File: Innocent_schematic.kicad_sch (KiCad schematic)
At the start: 59 parts, among them IC1 MP2338GTL-Z, J1 Conn_02x16_Top_Bottom, P1 USB_C_Plug_USB2.0, Q1 TIP42C, Q2 MMBT5551, Q3 MMBT5551, Q4 TIP42C, SW1 SPDT, U1 CH224K, U2 TP4056-42-ESOP8, U3 MP3423GG-Z, U4 RT6150AGQW, U5 INA219AxD, U6 DRV8833PWP, U7 DRV8833PWP

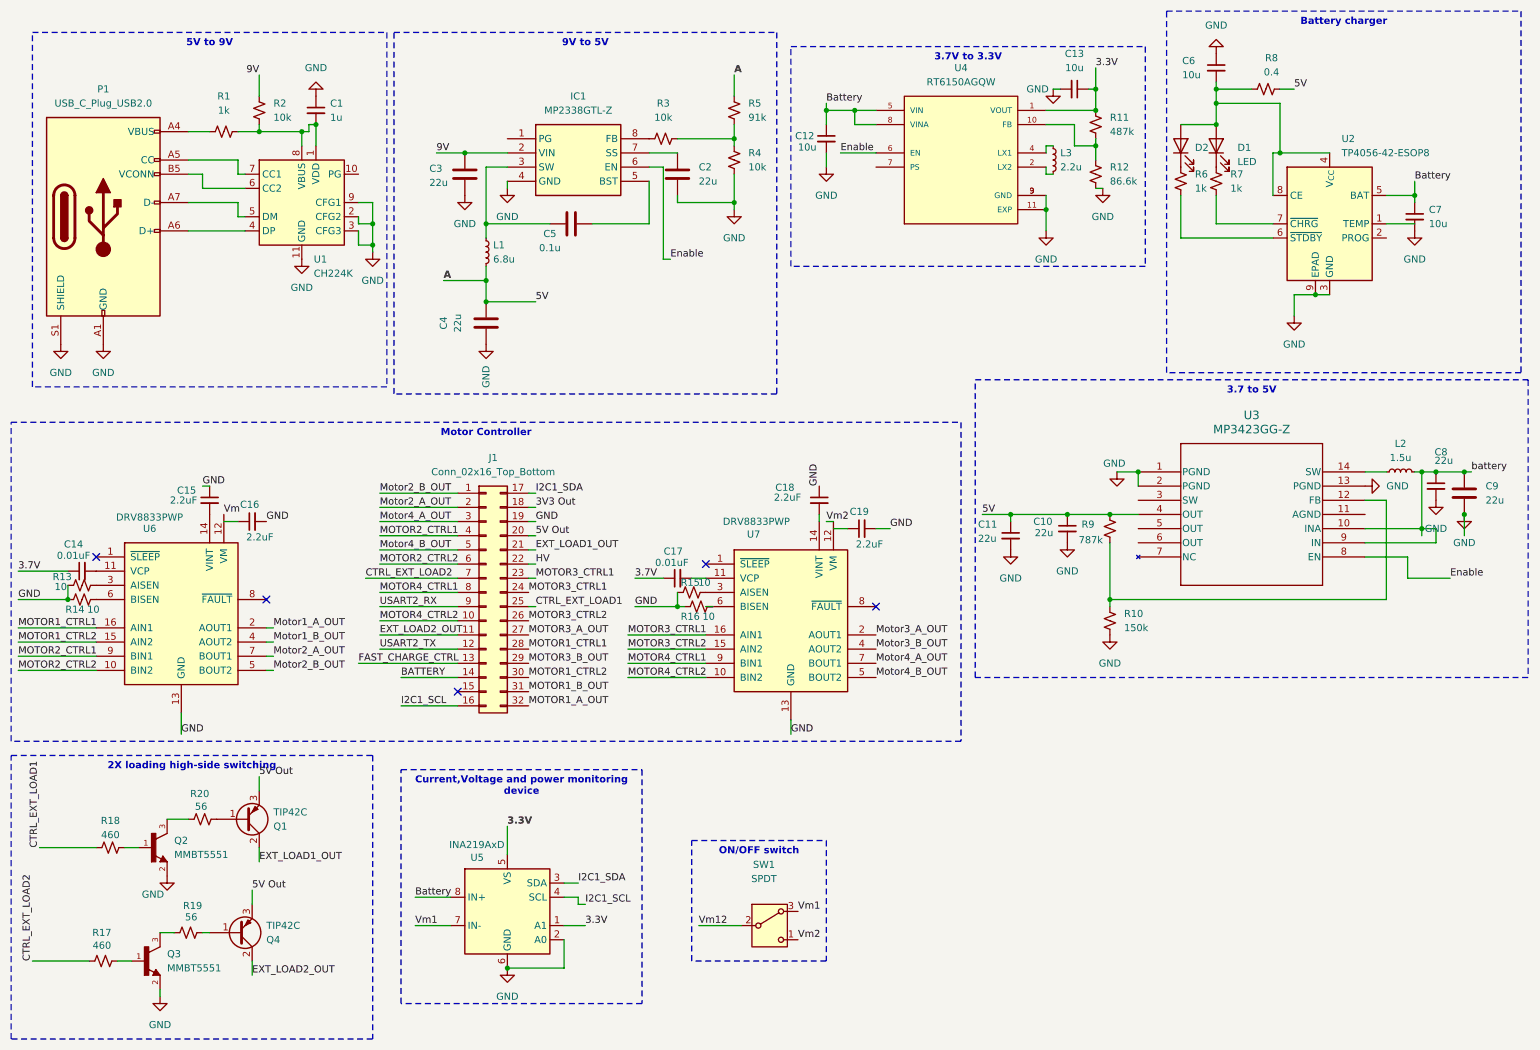
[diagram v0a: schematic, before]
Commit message: this version has pin numbers modified as we have analized and agreed
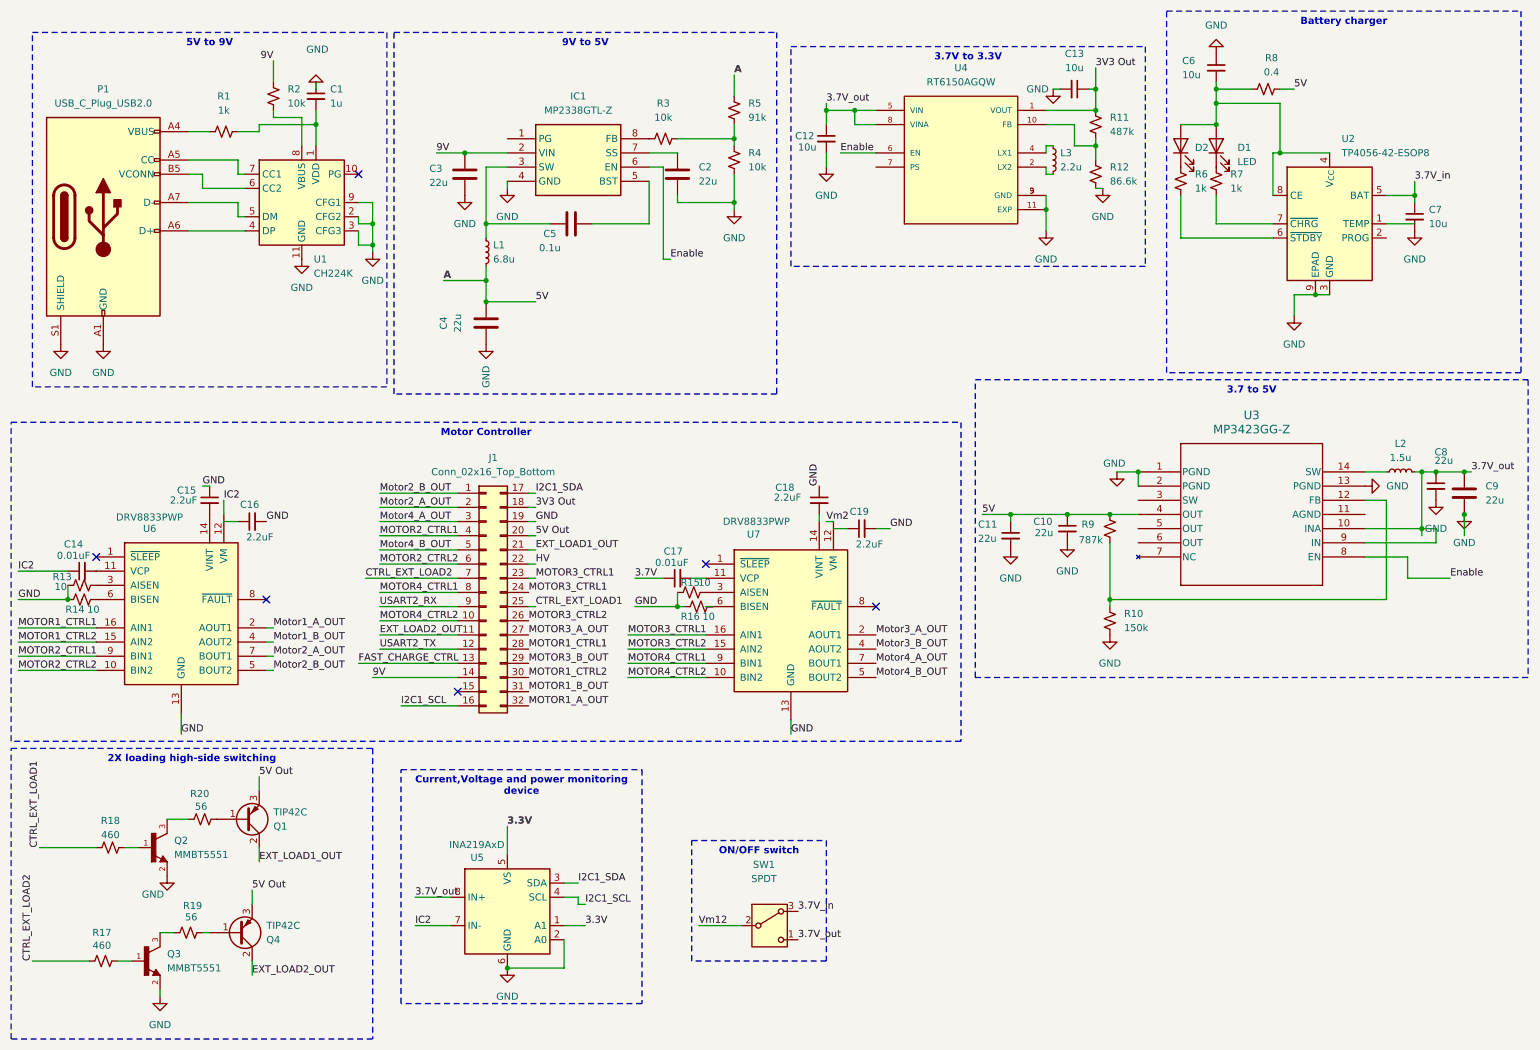
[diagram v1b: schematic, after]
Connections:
- net BATTERY is gone; now on net 9V: J1.14 (Pin_14)
- net battery is gone; now on net 3.7V_out: C8.1, C9.1, L2.2, U3.10 (INA), U3.9 (IN)
- net 3.3V: no longer C13.1, R11.1, U4.1 (VOUT)
- net 3.7V: no longer C14.1
- net 3V3 Out: now also C13.1, R11.1, U4.1 (VOUT)
- net Vm2: no longer SW1.1 (C)
- net at C1.2, R1.2, U1.1 (VDD): no longer R2.2, U1.8 (VBUS)
- net Battery renamed 3.7V_out
- net 3.7V_out: now also SW1.1 (C); no longer C7.1, U2.5 (BAT)
- net Vm renamed IC2
- net IC2: now also C14.1, U5.7 (IN-)
- net Vm1 renamed 3.7V_in
- net 3.7V_in: now also C7.1, U2.5 (BAT); no longer U5.7 (IN-)
- new net: R2.2, U1.8 (VBUS)
- no-connect marks 5 -> 6
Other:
- company: (none) -> University of Cape Town
- title: (none) -> EEE3088F_Micromouse_power_module
- moved on the sheet: C1, R2
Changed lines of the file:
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@@
 	(generator_version "9.0")
 	(paper "A4")
+	(title_block
+		(title "EEE3088F_Micromouse_power_module")
+		(date "2025-03-24")
+		(rev "R5")
+		(company "University of Cape Town")
+		(comment 1 "Authors: Rasekoai Mokose and Innocent Mkhonta")
+	)
 	(text_box "Battery charger"
 		(exclude_from_sim no)
@@
 	(text_box "2X loading high-side switching "
 		(exclude_from_sim no)
-		(at 12.7 146.05 0)
-		(size 64.77 50.8)
+		(at 12.7 144.78 0)
+		(size 64.77 52.07)
 		(margins 0.9525 0.9525 0.9525 0.9525)
 		(stroke
@@
 	)
 	(junction
-		(at 64.77 34.29)
-		(diameter 0)
-		(color 0 0 0 0)
-	)
-	(junction
 		(at 207.01 30.48)
 		(diameter 0)
@@
 	)
 	(junction
-		(at 57.15 34.29)
-		(diameter 0)
-		(color 0 0 0 0)
-	)
-	(junction
 		(at 246.38 63.5)
 		(diameter 0)
@@
 	)
 	(no_connect
+		(at 74.93 41.91)
+	)
+	(no_connect
 		(at 92.71 134.62)
 	)
@@
 	(wire
 		(pts
+			(xy 64.77 31.75) (xy 64.77 36.83)
+		)
+		(stroke
+			(width 0)
+			(type default)
+		)
+	)
+	(wire
+		(pts
 			(xy 123.19 127) (xy 137.16 127)
 		)
@@
 	(wire
 		(pts
-			(xy 64.77 36.83) (xy 64.77 34.29)
+			(xy 59.69 31.75) (xy 59.69 30.48)
 		)
 		(stroke
@@
 	(wire
 		(pts
-			(xy 64.77 34.29) (xy 57.15 34.29)
-		)
-		(stroke
-			(width 0)
-			(type default)
-		)
-	)
-	(wire
-		(pts
 			(xy 59.69 123.19) (xy 58.42 123.19)
 		)
@@
 	(wire
 		(pts
+			(xy 59.69 21.59) (xy 59.69 25.4)
+		)
+		(stroke
+			(width 0)
+			(type default)
+		)
+	)
+	(wire
+		(pts
 			(xy 116.84 50.8) (xy 127 50.8)
 		)
@@
 	(wire
 		(pts
+			(xy 67.31 30.48) (xy 67.31 33.02)
+		)
+		(stroke
+			(width 0)
+			(type default)
+		)
+	)
+	(wire
+		(pts
 			(xy 142.24 33.02) (xy 142.24 35.56)
 		)
@@
 	(wire
 		(pts
-			(xy 66.04 34.29) (xy 64.77 34.29)
-		)
-		(stroke
-			(width 0)
-			(type default)
-		)
-	)
-	(wire
-		(pts
 			(xy 134.62 114.3) (xy 137.16 114.3)
 		)
@@
 	(wire
 		(pts
+			(xy 67.31 25.4) (xy 67.31 26.67)
+		)
+		(stroke
+			(width 0)
+			(type default)
+		)
+	)
+	(wire
+		(pts
 			(xy 106.68 101.6) (xy 105.41 101.6)
 		)
@@
 	(wire
 		(pts
-			(xy 199.39 26.67) (xy 200.66 26.67)
+			(xy 59.69 31.75) (xy 64.77 31.75)
 		)
 		(stroke
@@
 	(wire
 		(pts
-			(xy 158.75 33.02) (xy 158.75 30.48)
+			(xy 199.39 26.67) (xy 200.66 26.67)
 		)
 		(stroke
@@
 	(wire
 		(pts
-			(xy 264.16 43.18) (xy 264.16 45.72)
+			(xy 158.75 33.02) (xy 158.75 30.48)
 		)
 		(stroke
@@
 	(wire
 		(pts
-			(xy 57.15 24.13) (xy 57.15 27.94)
+			(xy 264.16 43.18) (xy 264.16 45.72)
 		)
 		(stroke
@@
 	(wire
 		(pts
+			(xy 50.8 100.33) (xy 50.8 102.87)
+		)
+		(stroke
+			(width 0)
+			(type default)
+		)
+	)
+	(wire
+		(pts
 			(xy 273.05 95.25) (xy 274.32 95.25)
 		)
@@
 	(wire
 		(pts
+			(xy 57.15 33.02) (xy 67.31 33.02)
+		)
+		(stroke
+			(width 0)
+			(type default)
+		)
+	)
+	(wire
+		(pts
 			(xy 259.08 118.11) (xy 209.55 118.11)
 		)
@@
 	(wire
 		(pts
-			(xy 66.04 33.02) (xy 67.31 33.02)
-		)
-		(stroke
-			(width 0)
-			(type default)
-		)
-	)
-	(wire
-		(pts
 			(xy 142.24 35.56) (xy 142.24 36.83)
 		)
@@
 	(wire
 		(pts
-			(xy 66.04 33.02) (xy 66.04 34.29)
-		)
-		(stroke
-			(width 0)
-			(type default)
-		)
-	)
-	(wire
-		(pts
 			(xy 13.97 118.11) (xy 22.86 118.11)
 		)
@@
 	(wire
 		(pts
-			(xy 82.55 132.08) (xy 92.71 132.08)
+			(xy 77.47 132.08) (xy 92.71 132.08)
 		)
 		(stroke
@@
 		)
 	)
+	(label "9V"
+		(at 59.69 21.59 180)
+		(effects
+			(font
+				(size 1.27 1.27)
+			)
+			(justify right bottom)
+		)
+	)
 	(label "Motor4_B_OUT"
 		(at 167.64 132.08 0)
@@
 		)
 	)
-	(label "Battery"
+	(label "3.7V_in"
 		(at 264.16 43.18 0)
 		(effects
@@
 		)
 	)
-	(label "Vm1"
+	(label "3.7V_in"
 		(at 153.67 173.99 0)
 		(effects
@@
 		)
 	)
-	(label "Vm"
-		(at 50.8 102.87 0)
+	(label "IC2"
+		(at 50.8 100.33 0)
 		(effects
 			(font
@@
 		)
 	)
-	(label "Battery"
+	(label "3.7V_out"
 		(at 85.09 171.45 0)
 		(effects
@@
 		)
 	)
-	(label "Battery"
+	(label "3.7V_out"
 		(at 158.75 29.21 0)
 		(effects
@@
 		)
 	)
-	(label "3.3V"
+	(label "3V3 Out"
 		(at 207.01 22.86 0)
 		(effects
@@
 		)
 	)
-	(label "Vm2"
+	(label "3.7V_out"
 		(at 153.67 179.07 0)
 		(effects
@@
 		)
 	)
-	(label "3.7V"
+	(label "IC2"
 		(at 13.97 113.03 0)
 		(effects
@@
 		)
 	)
-	(label "Vm1"
+	(label "IC2"
 		(at 85.09 176.53 0)
 		(effects
@@
 		)
 	)
-	(label "9V"
-		(at 57.15 24.13 180)
-		(effects
-			(font
-				(size 1.27 1.27)
-			)
-			(justify right bottom)
-		)
-	)
-	(label "battery"
+	(label "3.7V_out"
 		(at 274.32 95.25 0)
 		(effects
@@
 		)
 	)
-	(label "BATTERY"
-		(at 82.55 132.08 0)
+	(label "9V"
+		(at 77.47 132.08 0)
 		(effects
 			(font
@@
 	(symbol
 		(lib_id "Device:C_Small")
-		(at 67.31 30.48 0)
+		(at 67.31 27.94 0)
 		(unit 1)
 		(exclude_from_sim no)
@@
 		(fields_autoplaced yes)
 		(property "Reference" "C1"
-			(at 69.85 29.2162 0)
+			(at 69.85 26.6762 0)
 			(effects
 				(font
@@
 		)
 		(property "Value" "1u"
-			(at 69.85 31.7562 0)
+			(at 69.85 29.2162 0)
 			(effects
 				(font
@@
 		)
 		(property "Footprint" ""
-			(at 67.31 30.48 0)
+			(at 67.31 27.94 0)
 			(effects
 				(font
@@
 		)
 		(property "Datasheet" "~"
-			(at 67.31 30.48 0)
+			(at 67.31 27.94 0)
 			(effects
 				(font
@@
 		)
 		(property "Description" "Unpolarized capacitor, small symbol"
-			(at 67.31 30.48 0)
+			(at 67.31 27.94 0)
 			(effects
 				(font
@@
 	(symbol
 		(lib_id "power:GND")
-		(at 67.31 27.94 180)
+		(at 67.31 26.67 180)
 		(unit 1)
 		(exclude_from_sim no)
@@
 		(on_board yes)
 		(dnp no)
-		(fields_autoplaced yes)
 		(property "Reference" "#PWR02"
-			(at 67.31 21.59 0)
+			(at 67.31 20.32 0)
 			(effects
 				(font
@@
 		)
 		(property "Value" "GND"
-			(at 67.31 22.86 0)
+			(at 67.564 19.558 0)
 			(effects
 				(font
@@
 		)
 		(property "Footprint" ""
-			(at 67.31 27.94 0)
+			(at 67.31 26.67 0)
 			(effects
 				(font
@@
 		)
 		(property "Datasheet" ""
-			(at 67.31 27.94 0)
+			(at 67.31 26.67 0)
 			(effects
 				(font
@@
 		)
 		(property "Description" "Power symbol creates a global label with name \"GND\" , ground"
-			(at 67.31 27.94 0)
+			(at 67.31 26.67 0)
 			(effects
 				(font
@@
 	(symbol
 		(lib_id "Device:R_Small_US")
-		(at 57.15 30.48 0)
+		(at 59.69 27.94 0)
 		(unit 1)
 		(exclude_from_sim no)
@@
 		(fields_autoplaced yes)
 		(property "Reference" "R2"
-			(at 59.69 29.2099 0)
+			(at 62.23 26.6699 0)
 			(effects
 				(font
@@
 		)
 		(property "Value" "10k"
-			(at 59.69 31.7499 0)
+			(at 62.23 29.2099 0)
 			(effects
 				(font
@@
 		)
 		(property "Footprint" ""
-			(at 57.15 30.48 0)
+			(at 59.69 27.94 0)
 			(effects
 				(font
@@
 		)
 		(property "Datasheet" "~"
-			(at 57.15 30.48 0)
+			(at 59.69 27.94 0)
 			(effects
 				(font
@@
 		)
 		(property "Description" "Resistor, small US symbol"
-			(at 57.15 30.48 0)
+			(at 59.69 27.94 0)
 			(effects
 				(font
@@
 		)
 		(instances
-			(project ""
+			(project "Innocent_schematic"
 				(path "/0ebc6b21-534b-4d26-a743-fadd30dffdd1"
 					(reference "R2")

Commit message: i have added the footprints to the folder and assigned most components, i am just left with JST pin and USB
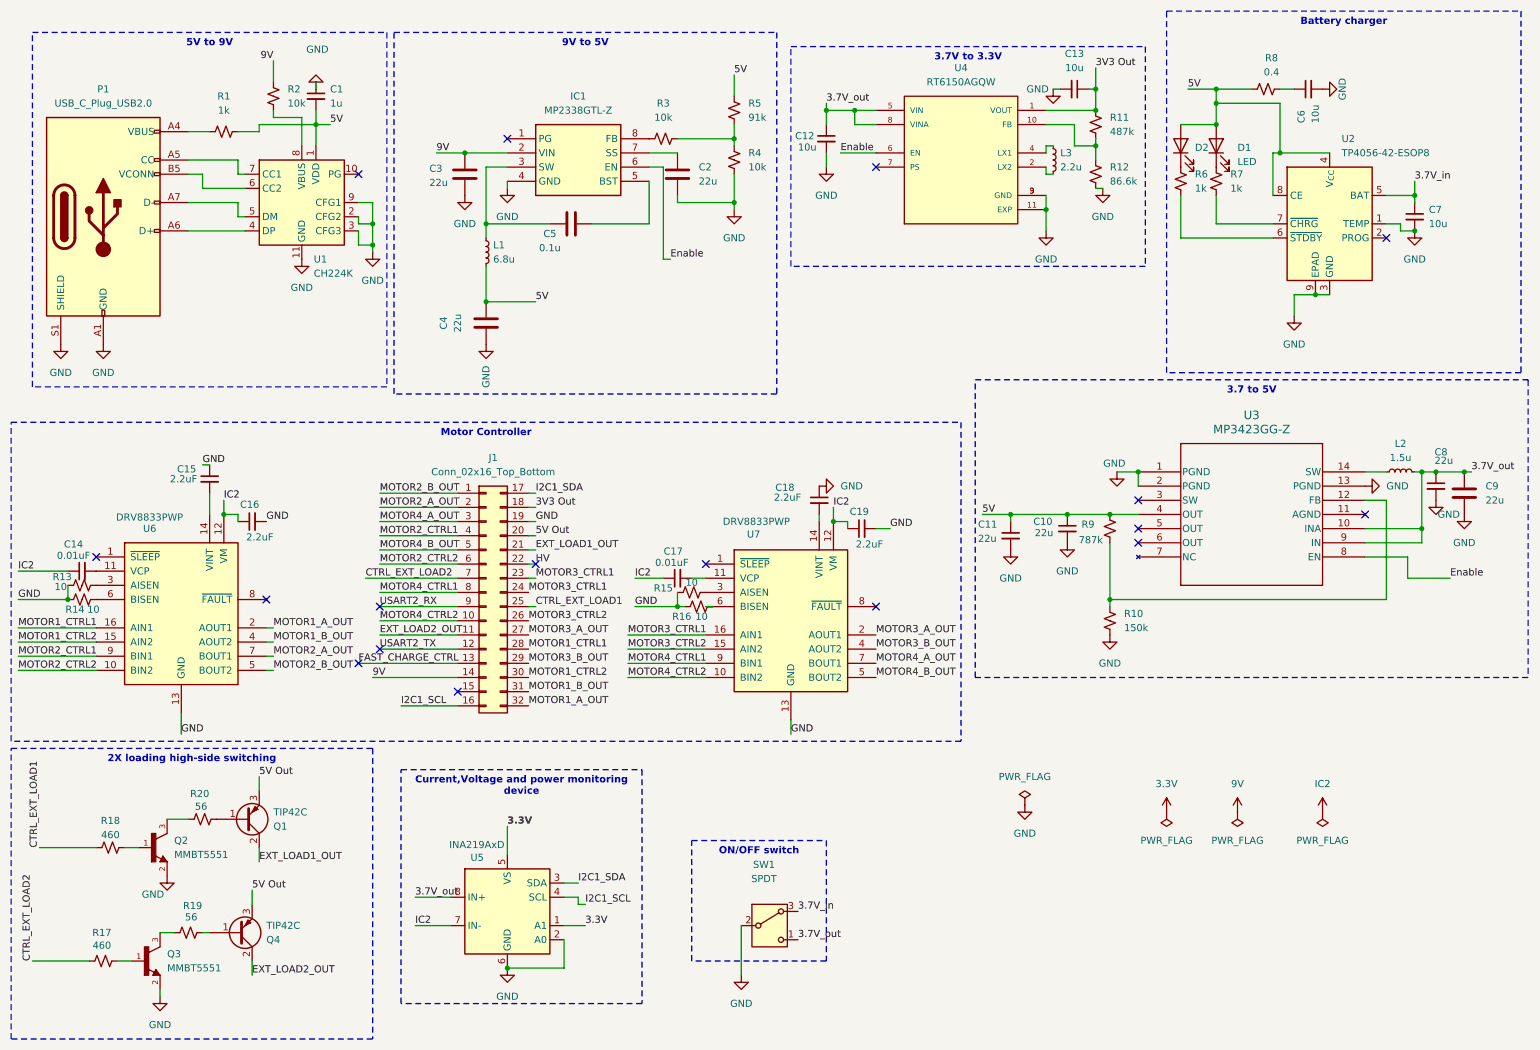
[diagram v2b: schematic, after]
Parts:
- IC1: footprint MP2338GTLZ -> (none)
- U3: footprint QFN14_MP3423_MNP -> (none)
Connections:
- net 3.7V is gone; now on net IC2: C17.1
- net Motor1_A_OUT is gone; now on net MOTOR1_A_OUT: U6.2 (AOUT1)
- net Motor1_B_OUT is gone; now on net MOTOR1_B_OUT: U6.4 (AOUT2)
- net Motor3_A_OUT is gone; now on net MOTOR3_A_OUT: U7.2 (AOUT1)
- net Motor3_B_OUT is gone; now on net MOTOR3_B_OUT: U7.4 (AOUT2)
- net Vm12 is gone; now on net GND: SW1.2 (B)
- net Vm2 is gone; now on net IC2: U7.12 (VM)
- net 5V: now also C1.2, D1.2 (A), D2.2 (A), R1.2, R8.2, U1.1 (VDD), U2.4 (V_{CC}), U2.8 (CE); no longer R8.1
- net GND: now also C6.2, U2.1 (TEMP); no longer C6.1
- net IC2: now also C16.1, C19.1
- net Motor2_A_OUT renamed MOTOR2_A_OUT
- net Motor2_B_OUT renamed MOTOR2_B_OUT
- net Motor4_A_OUT renamed MOTOR4_A_OUT
- net Motor4_B_OUT renamed MOTOR4_B_OUT
- new net: C6.1, R8.1
- no-connect marks 6 -> 17
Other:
- moved on the sheet: C15, C6
